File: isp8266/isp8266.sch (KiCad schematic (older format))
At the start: 69 parts, among them J1 S0, J10 9V_IN, J11 USB_C_Receptacle, J12 F0, J2 S2, J3 S1, J4 S3, J5 IMU, J6 USART, J7 F1, J8 BATTERY, J9 I2C, Q1 S8050, Q2 S8050, Q3 IRLML0030, Q4 IRLML6402, Q5 IRLML0030, Q6 IRLML6402, SW1 SW_Push, SW2 SW_Push, U1 CH340C, U2 AP1117-33, U3 IP5306, U4 ESP-12E

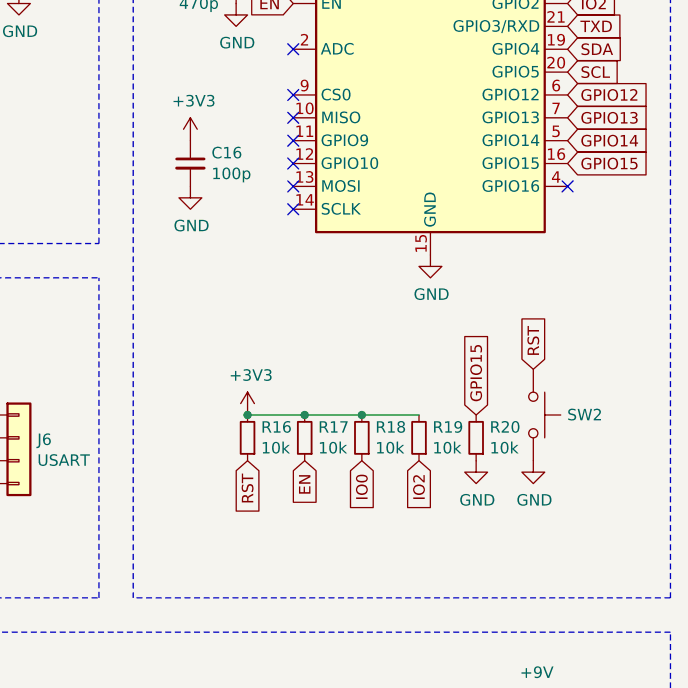
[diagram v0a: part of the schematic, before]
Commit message: Add IO0 button
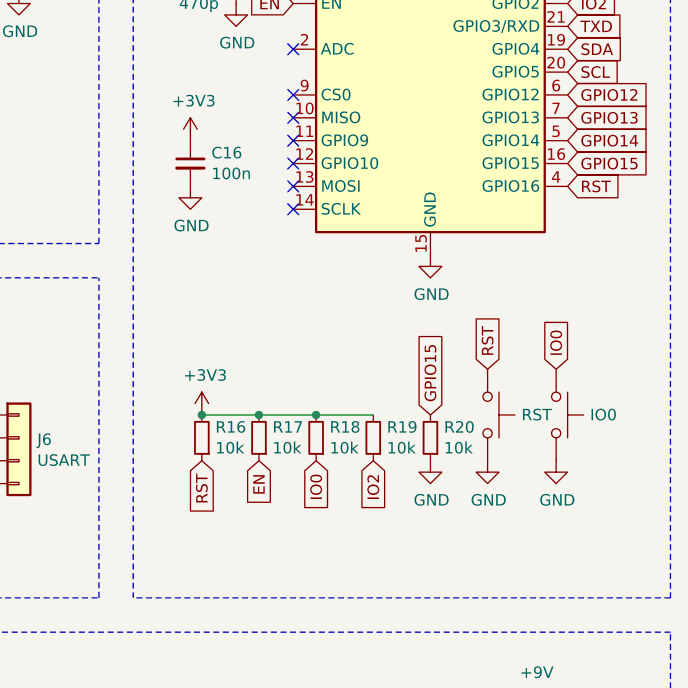
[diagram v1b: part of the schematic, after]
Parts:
- added IO0: SW_Push, symbol Switch:SW_Push
- C16: value 100p -> 100n
- renumbered SW2 to RST
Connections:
- net -BATT: now also IO0.2
- net IO0: now also IO0.1
- net RST: now also U4.4 (GPIO16)
- no-connect marks 15 -> 14
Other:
- moved on the sheet: R16, R17, R18, R19, R20, RST
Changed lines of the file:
@@
 Text GLabel 10150 1900 2    50   Input ~ 0
 GPIO14
-NoConn ~ 10150 2100
 Text GLabel 10150 1600 2    50   Input ~ 0
 SCL
@@
 P 8500 2000
 F 0 "C16" H 8592 2046 50  0000 L CNN
-F 1 "100p" H 8592 1955 50  0000 L CNN
+F 1 "100n" H 8592 1955 50  0000 L CNN
 F 2 "Capacitor_SMD:C_0603_1608Metric" H 8500 2000 50  0001 C CNN
 F 3 "~" H 8500 2000 50  0001 C CNN
@@
 L power:GND #PWR054
 U 1 1 639466D7
-P 10000 3300
-F 0 "#PWR054" H 10000 3050 50  0001 C CNN
-F 1 "GND" H 10005 3127 50  0000 C CNN
-F 2 "" H 10000 3300 50  0001 C CNN
-F 3 "" H 10000 3300 50  0001 C CNN
-	1    10000 3300
-	1    0    0    -1
-$EndComp
-Text GLabel 10000 2900 1    50   Input ~ 0
+P 9800 3300
+F 0 "#PWR054" H 9800 3050 50  0001 C CNN
+F 1 "GND" H 9805 3127 50  0000 C CNN
+F 2 "" H 9800 3300 50  0001 C CNN
+F 3 "" H 9800 3300 50  0001 C CNN
+	1    9800 3300
+	1    0    0    -1
+$EndComp
+Text GLabel 9800 2900 1    50   Input ~ 0
 RST
-$Comp
-L Switch:SW_Push SW2
-U 1 1 6393B888
-P 10000 3100
-F 0 "SW2" V 10000 3248 50  0000 L CNN
-F 1 "SW_Push" V 10045 3248 50  0001 L CNN
-F 2 "" H 10000 3300 50  0001 C CNN
-F 3 "~" H 10000 3300 50  0001 C CNN
-	1    10000 3100
-	0    1    1    0
-$EndComp
 $Comp
 L power:GND #PWR052
 U 1 1 638FE496
-P 9750 3300
-F 0 "#PWR052" H 9750 3050 50  0001 C CNN
-F 1 "GND" H 9755 3127 50  0000 C CNN
-F 2 "" H 9750 3300 50  0001 C CNN
-F 3 "" H 9750 3300 50  0001 C CNN
-	1    9750 3300
+P 9550 3300
+F 0 "#PWR052" H 9550 3050 50  0001 C CNN
+F 1 "GND" H 9555 3127 50  0000 C CNN
+F 2 "" H 9550 3300 50  0001 C CNN
+F 3 "" H 9550 3300 50  0001 C CNN
+	1    9550 3300
 	1    0    0    -1
 $EndComp
@@
 L Device:R_Small R20
 U 1 1 638FCAE7
-P 9750 3200
-F 0 "R20" H 9691 3154 50  0000 R CNN
-F 1 "10k" H 9691 3245 50  0000 R CNN
-F 2 "Resistor_SMD:R_0603_1608Metric" H 9750 3200 50  0001 C CNN
-F 3 "~" H 9750 3200 50  0001 C CNN
-	1    9750 3200
+P 9550 3200
+F 0 "R20" H 9491 3154 50  0000 R CNN
+F 1 "10k" H 9491 3245 50  0000 R CNN
+F 2 "Resistor_SMD:R_0603_1608Metric" H 9550 3200 50  0001 C CNN
+F 3 "~" H 9550 3200 50  0001 C CNN
+	1    9550 3200
 	-1   0    0    1
 $EndComp
-Text GLabel 9750 3100 1    50   Input ~ 0
+Text GLabel 9550 3100 1    50   Input ~ 0
 GPIO15
-Text GLabel 9000 3300 3    50   Input ~ 0
+Text GLabel 8800 3300 3    50   Input ~ 0
 EN
-Text GLabel 9500 3300 3    50   Input ~ 0
+Text GLabel 9300 3300 3    50   Input ~ 0
 IO2
-Text GLabel 9250 3300 3    50   Input ~ 0
+Text GLabel 9050 3300 3    50   Input ~ 0
 IO0
-Text GLabel 8750 3300 3    50   Input ~ 0
+Text GLabel 8550 3300 3    50   Input ~ 0
 RST
 Wire Wire Line
-	9250 3100 9500 3100
-Connection ~ 9250 3100
-Wire Wire Line
-	9000 3100 9250 3100
-Connection ~ 9000 3100
-Connection ~ 8750 3100
-Wire Wire Line
-	8750 3100 9000 3100
+	9050 3100 9300 3100
+Connection ~ 9050 3100
+Wire Wire Line
+	8800 3100 9050 3100
+Connection ~ 8800 3100
+Connection ~ 8550 3100
+Wire Wire Line
+	8550 3100 8800 3100
 $Comp
 L power:+3V3 #PWR049
 U 1 1 63915960
-P 8750 3100
-F 0 "#PWR049" H 8750 2950 50  0001 C CNN
-F 1 "+3V3" H 8765 3273 50  0000 C CNN
-F 2 "" H 8750 3100 50  0001 C CNN
-F 3 "" H 8750 3100 50  0001 C CNN
-	1    8750 3100
+P 8550 3100
+F 0 "#PWR049" H 8550 2950 50  0001 C CNN
+F 1 "+3V3" H 8565 3273 50  0000 C CNN
+F 2 "" H 8550 3100 50  0001 C CNN
+F 3 "" H 8550 3100 50  0001 C CNN
+	1    8550 3100
 	1    0    0    -1
 $EndComp
@@
 L Device:R_Small R19
 U 1 1 63909811
-P 9500 3200
-F 0 "R19" H 9441 3154 50  0000 R CNN
-F 1 "10k" H 9441 3245 50  0000 R CNN
-F 2 "Resistor_SMD:R_0603_1608Metric" H 9500 3200 50  0001 C CNN
-F 3 "~" H 9500 3200 50  0001 C CNN
-	1    9500 3200
+P 9300 3200
+F 0 "R19" H 9241 3154 50  0000 R CNN
+F 1 "10k" H 9241 3245 50  0000 R CNN
+F 2 "Resistor_SMD:R_0603_1608Metric" H 9300 3200 50  0001 C CNN
+F 3 "~" H 9300 3200 50  0001 C CNN
+	1    9300 3200
 	-1   0    0    1
 $EndComp
@@
 L Device:R_Small R18
 U 1 1 63908DDD
-P 9250 3200
-F 0 "R18" H 9191 3154 50  0000 R CNN
-F 1 "10k" H 9191 3245 50  0000 R CNN
-F 2 "Resistor_SMD:R_0603_1608Metric" H 9250 3200 50  0001 C CNN
-F 3 "~" H 9250 3200 50  0001 C CNN
-	1    9250 3200
+P 9050 3200
+F 0 "R18" H 8991 3154 50  0000 R CNN
+F 1 "10k" H 8991 3245 50  0000 R CNN
+F 2 "Resistor_SMD:R_0603_1608Metric" H 9050 3200 50  0001 C CNN
+F 3 "~" H 9050 3200 50  0001 C CNN
+	1    9050 3200
 	-1   0    0    1
 $EndComp
@@
 L Device:R_Small R17
 U 1 1 639077CF
-P 9000 3200
-F 0 "R17" H 8941 3154 50  0000 R CNN
-F 1 "10k" H 8941 3245 50  0000 R CNN
-F 2 "Resistor_SMD:R_0603_1608Metric" H 9000 3200 50  0001 C CNN
-F 3 "~" H 9000 3200 50  0001 C CNN
-	1    9000 3200
+P 8800 3200
+F 0 "R17" H 8741 3154 50  0000 R CNN
+F 1 "10k" H 8741 3245 50  0000 R CNN
+F 2 "Resistor_SMD:R_0603_1608Metric" H 8800 3200 50  0001 C CNN
+F 3 "~" H 8800 3200 50  0001 C CNN
+	1    8800 3200
 	-1   0    0    1
 $EndComp
@@
 L Device:R_Small R16
 U 1 1 63907406
-P 8750 3200
-F 0 "R16" H 8691 3154 50  0000 R CNN
-F 1 "10k" H 8691 3245 50  0000 R CNN
-F 2 "Resistor_SMD:R_0603_1608Metric" H 8750 3200 50  0001 C CNN
-F 3 "~" H 8750 3200 50  0001 C CNN
-	1    8750 3200
+P 8550 3200
+F 0 "R16" H 8491 3154 50  0000 R CNN
+F 1 "10k" H 8491 3245 50  0000 R CNN
+F 2 "Resistor_SMD:R_0603_1608Metric" H 8550 3200 50  0001 C CNN
+F 3 "~" H 8550 3200 50  0001 C CNN
+	1    8550 3200
 	-1   0    0    1
 $EndComp
@@
 Text GLabel 7600 4650 1    50   Input ~ 0
 Vf
+Text GLabel 10150 2100 2    50   Input ~ 0
+RST
+$Comp
+L power:GND #PWR?
+U 1 1 6399AD99
+P 10100 3300
+F 0 "#PWR?" H 10100 3050 50  0001 C CNN
+F 1 "GND" H 10105 3127 50  0000 C CNN
+F 2 "" H 10100 3300 50  0001 C CNN
+F 3 "" H 10100 3300 50  0001 C CNN
+	1    10100 3300
+	1    0    0    -1
+$EndComp
+Text GLabel 10100 2900 1    50   Input ~ 0
+IO0
+$Comp
+L Switch:SW_Push IO0
+U 1 1 6399ADA0
+P 10100 3100
+F 0 "IO0" V 10100 3248 50  0000 L CNN
+F 1 "SW_Push" V 10145 3248 50  0001 L CNN
+F 2 "" H 10100 3300 50  0001 C CNN
+F 3 "~" H 10100 3300 50  0001 C CNN
+	1    10100 3100
+	0    1    1    0
+$EndComp
+$Comp
+L Switch:SW_Push RST
+U 1 1 6393B888
+P 9800 3100
+F 0 "RST" V 9800 3248 50  0000 L CNN
+F 1 "SW_Push" V 9845 3248 50  0001 L CNN
+F 2 "" H 9800 3300 50  0001 C CNN
+F 3 "~" H 9800 3300 50  0001 C CNN
+	1    9800 3100
+	0    1    1    0
+$EndComp
 $EndSCHEMATC

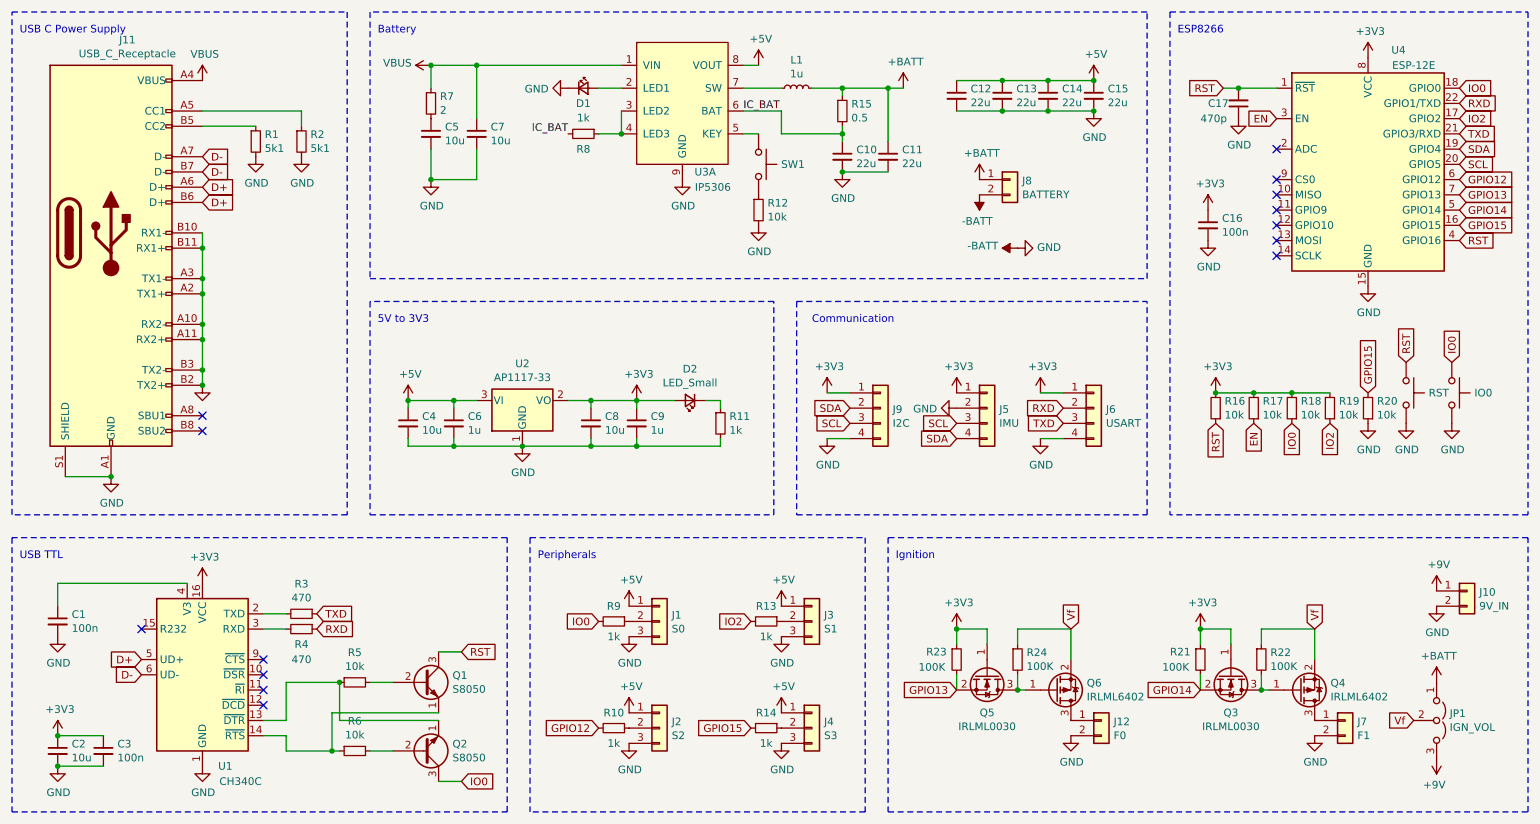
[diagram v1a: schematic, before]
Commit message: Modify NMOS and footprint
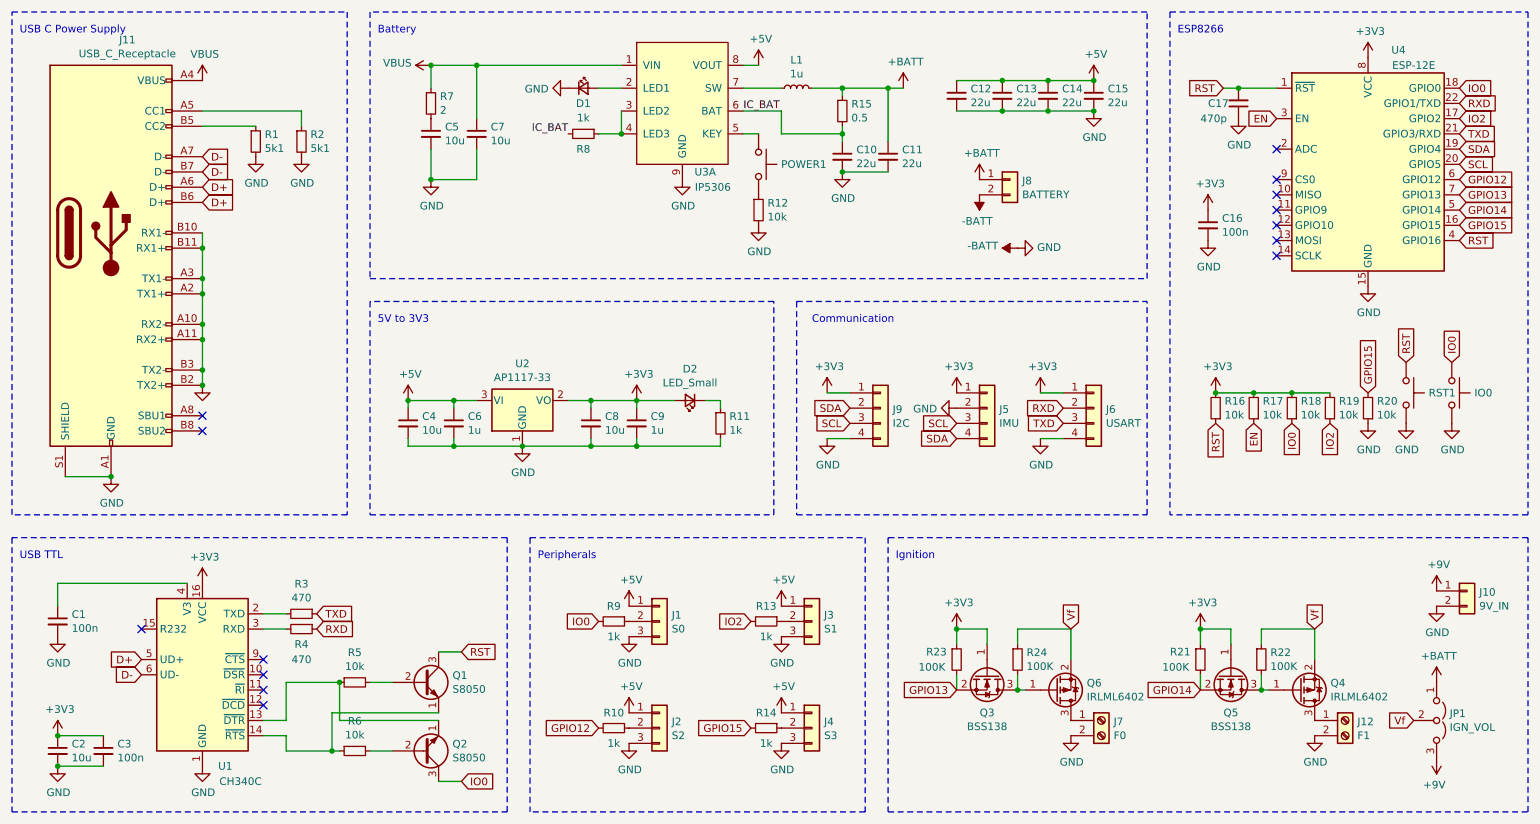
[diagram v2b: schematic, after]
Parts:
- removed J12: F0, symbol Connector_Generic:Conn_01x02
- removed J7: F1, symbol Connector_Generic:Conn_01x02
- removed Q3, Q5: IRLML0030, Package_TO_SOT_SMD:SOT-23, symbol Transistor_FET:IRLML0030
- added J12: F1, TerminalBlock_Phoenix:TerminalBlock_Phoenix_MPT-0,5-2-2.54_1x02_P2.54mm_Horizontal, symbol Connector:Screw_Terminal_01x02
- added J7: F0, TerminalBlock_Phoenix:TerminalBlock_Phoenix_MPT-0,5-2-2.54_1x02_P2.54mm_Horizontal, symbol Connector:Screw_Terminal_01x02
- added Q3, Q5: BSS138, Package_TO_SOT_SMD:SOT-23, symbol Transistor_FET:BSS138
- IO0: footprint (none) -> Button_Switch_SMD:SW_SPST_B3U-1000P
- J10: footprint (none) -> Connector_Molex:Molex_KK-254_AE-6410-02A_1x02_P2.54mm_Vertical
- JP1: footprint (none) -> Connector_PinSocket_2.54mm:PinSocket_1x03_P2.54mm_Vertical
- POWER1: renamed from SW1; footprint (none) -> Button_Switch_SMD:SW_SPST_EVQPE1
- R21, R22, R23, R24: footprint (none) -> Resistor_SMD:R_0603_1608Metric
- RST1: renamed from RST; footprint (none) -> Button_Switch_SMD:SW_SPST_EVQPE1
- U3: footprint (none) -> Package_SO:HTSOP-8-1EP_3.9x4.9mm_P1.27mm_EP2.4x3.2mm
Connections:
- net +3V3: now also Q3.1 (G), Q5.1 (G)
- net -BATT: now also J12.2 (Pin_2), J7.2 (Pin_2)
- net GPIO13: now also Q3.2 (S)
- net GPIO14: now also Q5.2 (S)
- net at Q6.1 (G), R24.2: now also Q3.3 (D)
- net at Q6.3 (D): now also J7.1 (Pin_1)
- net at Q4.1 (G), R22.2: now also Q5.3 (D)
- net at Q4.3 (D): now also J12.1 (Pin_1)
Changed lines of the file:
@@
 	5450 1400 5550 1400
 $Comp
-L Switch:SW_Push SW1
+L Switch:SW_Push POWER1
 U 1 1 6381ECE4
 P 5550 1600
-F 0 "SW1" V 5550 1748 50  0000 L CNN
+F 0 "POWER1" V 5550 1748 50  0000 L CNN
 F 1 "SW_Push" V 5595 1748 50  0001 L CNN
-F 2 "" H 5550 1800 50  0001 C CNN
+F 2 "Button_Switch_SMD:SW_SPST_EVQPE1" H 5550 1800 50  0001 C CNN
 F 3 "~" H 5550 1800 50  0001 C CNN
 	1    5550 1600
@@
 F 0 "U3" H 5200 750 50  0000 C CNN
 F 1 "IP5306" H 5250 650 50  0000 C CNN
-F 2 "" H 5050 1200 50  0001 C CNN
+F 2 "Package_SO:HTSOP-8-1EP_3.9x4.9mm_P1.27mm_EP2.4x3.2mm" H 5050 1200 50  0001 C CNN
 F 3 "" H 5050 1200 50  0001 C CNN
 	1    5050 1200
@@
 Text GLabel 5500 5300 0    50   Input ~ 0
 GPIO15
-$Comp
-L Transistor_FET:IRLML0030 Q5
-U 1 1 63860476
-P 7050 4950
-F 0 "Q5" V 7299 4950 50  0000 C CNN
-F 1 "IRLML0030" V 7390 4950 50  0000 C CNN
-F 2 "Package_TO_SOT_SMD:SOT-23" H 7250 4875 50  0001 L CIN
-F 3 "https://www.infineon.com/dgdl/irlml0030pbf.pdf?fileId=5546d462533600a401535664773825df" H 7050 4950 50  0001 L CNN
-	1    7050 4950
-	0    1    1    0
-$EndComp
 $Comp
 L Device:R_Small R23
@@
 F 0 "R23" H 6650 4900 50  0000 L CNN
 F 1 "100K" H 6600 4800 50  0000 L CNN
-F 2 "" H 6850 4850 50  0001 C CNN
+F 2 "Resistor_SMD:R_0603_1608Metric" H 6850 4850 50  0001 C CNN
 F 3 "~" H 6850 4850 50  0001 C CNN
 	1    6850 4850
@@
 F 0 "R24" H 7309 4896 50  0000 L CNN
 F 1 "100K" H 7309 4805 50  0000 L CNN
-F 2 "" H 7250 4850 50  0001 C CNN
+F 2 "Resistor_SMD:R_0603_1608Metric" H 7250 4850 50  0001 C CNN
 F 3 "~" H 7250 4850 50  0001 C CNN
 	1    7250 4850
@@
 	7600 4650 7600 4850
 $Comp
-L Connector_Generic:Conn_01x02 J12
-U 1 1 63897A37
-P 7800 5250
-F 0 "J12" H 7880 5242 50  0000 L CNN
-F 1 "F0" H 7880 5151 50  0000 L CNN
-F 2 "" H 7800 5250 50  0001 C CNN
-F 3 "~" H 7800 5250 50  0001 C CNN
-	1    7800 5250
-	1    0    0    -1
-$EndComp
-$Comp
 L power:GND #PWR056
 U 1 1 63898B12
@@
 Wire Wire Line
 	7250 4950 7250 5050
-Connection ~ 7250 5050
 Wire Wire Line
 	7250 4750 7250 4650
 Wire Wire Line
 	7250 4650 7600 4650
-$Comp
-L Transistor_FET:IRLML0030 Q3
-U 1 1 639260C9
-P 8650 4950
-F 0 "Q3" V 8899 4950 50  0000 C CNN
-F 1 "IRLML0030" V 8990 4950 50  0000 C CNN
-F 2 "Package_TO_SOT_SMD:SOT-23" H 8850 4875 50  0001 L CIN
-F 3 "https://www.infineon.com/dgdl/irlml0030pbf.pdf?fileId=5546d462533600a401535664773825df" H 8650 4950 50  0001 L CNN
-	1    8650 4950
-	0    1    1    0
-$EndComp
 $Comp
 L Device:R_Small R21
@@
 F 0 "R21" H 8250 4900 50  0000 L CNN
 F 1 "100K" H 8200 4800 50  0000 L CNN
-F 2 "" H 8450 4850 50  0001 C CNN
+F 2 "Resistor_SMD:R_0603_1608Metric" H 8450 4850 50  0001 C CNN
 F 3 "~" H 8450 4850 50  0001 C CNN
 	1    8450 4850
@@
 F 0 "R22" H 8909 4896 50  0000 L CNN
 F 1 "100K" H 8909 4805 50  0000 L CNN
-F 2 "" H 8850 4850 50  0001 C CNN
+F 2 "Resistor_SMD:R_0603_1608Metric" H 8850 4850 50  0001 C CNN
 F 3 "~" H 8850 4850 50  0001 C CNN
 	1    8850 4850
@@
 Wire Wire Line
 	8850 4950 8850 5050
-Connection ~ 8850 5050
 Wire Wire Line
 	8850 4750 8850 4650
@@
 F 3 "" H 9200 5350 50  0001 C CNN
 	1    9200 5350
-	1    0    0    -1
-$EndComp
-$Comp
-L Connector_Generic:Conn_01x02 J7
-U 1 1 639260EF
-P 9400 5250
-F 0 "J7" H 9480 5242 50  0000 L CNN
-F 1 "F1" H 9480 5151 50  0000 L CNN
-F 2 "" H 9400 5250 50  0001 C CNN
-F 3 "~" H 9400 5250 50  0001 C CNN
-	1    9400 5250
 	1    0    0    -1
 $EndComp
@@
 F 0 "J10" H 10280 4392 50  0000 L CNN
 F 1 "9V_IN" H 10280 4301 50  0000 L CNN
-F 2 "" H 10200 4400 50  0001 C CNN
+F 2 "Connector_Molex:Molex_KK-254_AE-6410-02A_1x02_P2.54mm_Vertical" H 10200 4400 50  0001 C CNN
 F 3 "~" H 10200 4400 50  0001 C CNN
 	1    10200 4400
@@
 F 0 "JP1" V 9954 5336 50  0000 L CNN
 F 1 "IGN_VOL" V 10045 5336 50  0000 L CNN
-F 2 "" H 10000 5250 50  0001 C CNN
+F 2 "Connector_PinSocket_2.54mm:PinSocket_1x03_P2.54mm_Vertical" H 10000 5250 50  0001 C CNN
 F 3 "~" H 10000 5250 50  0001 C CNN
 	1    10000 5250
@@
 RST
 $Comp
-L power:GND #PWR?
+L power:GND #PWR0104
 U 1 1 6399AD99
 P 10100 3300
-F 0 "#PWR?" H 10100 3050 50  0001 C CNN
+F 0 "#PWR0104" H 10100 3050 50  0001 C CNN
 F 1 "GND" H 10105 3127 50  0000 C CNN
 F 2 "" H 10100 3300 50  0001 C CNN
@@
 F 0 "IO0" V 10100 3248 50  0000 L CNN
 F 1 "SW_Push" V 10145 3248 50  0001 L CNN
-F 2 "" H 10100 3300 50  0001 C CNN
+F 2 "Button_Switch_SMD:SW_SPST_B3U-1000P" H 10100 3300 50  0001 C CNN
 F 3 "~" H 10100 3300 50  0001 C CNN
 	1    10100 3100
@@
 $EndComp
 $Comp
-L Switch:SW_Push RST
+L Switch:SW_Push RST1
 U 1 1 6393B888
 P 9800 3100
-F 0 "RST" V 9800 3248 50  0000 L CNN
+F 0 "RST1" V 9800 3248 50  0000 L CNN
 F 1 "SW_Push" V 9845 3248 50  0001 L CNN
-F 2 "" H 9800 3300 50  0001 C CNN
+F 2 "Button_Switch_SMD:SW_SPST_EVQPE1" H 9800 3300 50  0001 C CNN
 F 3 "~" H 9800 3300 50  0001 C CNN
 	1    9800 3100
 	0    1    1    0
 $EndComp
+$Comp
+L Connector:Screw_Terminal_01x02 J7
+U 1 1 638D8445
+P 7800 5250
+F 0 "J7" H 7880 5242 50  0000 L CNN
+F 1 "F0" H 7880 5151 50  0000 L CNN
+F 2 "TerminalBlock_Phoenix:TerminalBlock_Phoenix_MPT-0,5-2-2.54_1x02_P2.54mm_Horizontal" H 7800 5250 50  0001 C CNN
+F 3 "~" H 7800 5250 50  0001 C CNN
+	1    7800 5250
+	1    0    0    -1
+$EndComp
+$Comp
+L Connector:Screw_Terminal_01x02 J12
+U 1 1 638DBEDB
+P 9400 5250
+F 0 "J12" H 9480 5242 50  0000 L CNN
+F 1 "F1" H 9480 5151 50  0000 L CNN
+F 2 "TerminalBlock_Phoenix:TerminalBlock_Phoenix_MPT-0,5-2-2.54_1x02_P2.54mm_Horizontal" H 9400 5250 50  0001 C CNN
+F 3 "~" H 9400 5250 50  0001 C CNN
+	1    9400 5250
+	1    0    0    -1
+$EndComp
+$Comp
+L Transistor_FET:BSS138 Q3
+U 1 1 6392E3D4
+P 7050 4950
+F 0 "Q3" V 7299 4950 50  0000 C CNN
+F 1 "BSS138" V 7390 4950 50  0000 C CNN
+F 2 "Package_TO_SOT_SMD:SOT-23" H 7250 4875 50  0001 L CIN
+F 3 "https://www.onsemi.com/pub/Collateral/BSS138-D.PDF" H 7050 4950 50  0001 L CNN
+	1    7050 4950
+	0    1    1    0
+$EndComp
+Connection ~ 7250 5050
+$Comp
+L Transistor_FET:BSS138 Q5
+U 1 1 6393B8B2
+P 8650 4950
+F 0 "Q5" V 8899 4950 50  0000 C CNN
+F 1 "BSS138" V 8990 4950 50  0000 C CNN
+F 2 "Package_TO_SOT_SMD:SOT-23" H 8850 4875 50  0001 L CIN
+F 3 "https://www.onsemi.com/pub/Collateral/BSS138-D.PDF" H 8650 4950 50  0001 L CNN
+	1    8650 4950
+	0    1    1    0
+$EndComp
+Connection ~ 8850 5050
 $EndSCHEMATC

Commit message: Change I2C connector
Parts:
- J9: footprint Connector_PinSocket_2.54mm:PinSocket_1x04_P2.54mm_Horizontal -> Connector_PinSocket_2.54mm:PinSocket_1x04_P2.54mm_Vertical
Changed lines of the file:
@@
 F 0 "J9" H 6430 3192 50  0000 L CNN
 F 1 "I2C" H 6430 3101 50  0000 L CNN
-F 2 "Connector_PinSocket_2.54mm:PinSocket_1x04_P2.54mm_Horizontal" H 6350 3200 50  0001 C CNN
+F 2 "Connector_PinSocket_2.54mm:PinSocket_1x04_P2.54mm_Vertical" H 6350 3200 50  0001 C CNN
 F 3 "~" H 6350 3200 50  0001 C CNN
 	1    6350 3200
